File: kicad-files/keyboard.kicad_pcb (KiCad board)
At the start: 2 copper layers, 361.7 x 100 mm, 189 parts, among them J1 TYPE-C-31-M12_13, Q1 2N7002, Q2 2N7002, SW1 K2-1187SQ-A4SW-06, T1 53261-0471, T2 53261-0471, U1 STM32F411CEU6, U2 USBLC6-2SC6, U3 AT24C256C-SSHL-T, U4 SGM2007-3.3XN5/TR, Y1 TAXM8M4RFDCET2T

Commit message: More naming and filleted edge
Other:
- outline, holes or cut-outs redrawn
- board text added: "CAPS_LOCK"
- board text added: "MISC"
- board text added: "TAB"
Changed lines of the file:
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@@
   (gr_line locked (start 162.5 0) (end 162.5 100)
     (stroke (width 0.1) (type default)) (layer "Eco1.User"))
+  (gr_arc (start 1.5 2.1) (mid 2.964466 -1.435534) (end 6.5 -2.9)
+    (stroke (width 0.25) (type default)) (layer "Edge.Cuts"))
+  (gr_line (start 6.5 -2.9) (end 318.5 -2.9)
+    (stroke (width 0.25) (type default)) (layer "Edge.Cuts"))
   (gr_line (start 348.2 61) (end 348.2 36)
     (stroke (width 0.1) (type default)) (layer "Edge.Cuts"))
@@
   (gr_line (start 362.2 62) (end 349.2 62)
     (stroke (width 0.1) (type default)) (layer "Edge.Cuts"))
-  (gr_rect (start 1.5 -2.9) (end 323.5 97.1)
-    (stroke (width 0.25) (type default)) (fill none) (layer "Edge.Cuts"))
   (gr_arc (start 348.2 36) (mid 348.492893 35.292893) (end 349.2 35)
     (stroke (width 0.1) (type default)) (layer "Edge.Cuts"))
+  (gr_line (start 323.5 2.1) (end 323.5 92.1)
+    (stroke (width 0.25) (type default)) (layer "Edge.Cuts"))
+  (gr_arc (start 323.5 92.1) (mid 322.035534 95.635534) (end 318.5 97.1)
+    (stroke (width 0.25) (type default)) (layer "Edge.Cuts"))
   (gr_arc (start 349.2 62) (mid 348.492893 61.707107) (end 348.2 61)
     (stroke (width 0.1) (type default)) (layer "Edge.Cuts"))
   (gr_line (start 363.2 36) (end 363.2 61)
     (stroke (width 0.1) (type default)) (layer "Edge.Cuts"))
+  (gr_arc (start 318.5 -2.9) (mid 322.035534 -1.435534) (end 323.5 2.1)
+    (stroke (width 0.25) (type default)) (layer "Edge.Cuts"))
   (gr_arc (start 363.2 61) (mid 362.907107 61.707107) (end 362.2 62)
     (stroke (width 0.1) (type default)) (layer "Edge.Cuts"))
+  (gr_line (start 1.5 92.1) (end 1.5 2.1)
+    (stroke (width 0.25) (type default)) (layer "Edge.Cuts"))
+  (gr_arc (start 6.5 97.1) (mid 2.964466 95.635534) (end 1.5 92.1)
+    (stroke (width 0.25) (type default)) (layer "Edge.Cuts"))
   (gr_arc (start 362.2 35) (mid 362.907107 35.292893) (end 363.2 36)
     (stroke (width 0.1) (type default)) (layer "Edge.Cuts"))
+  (gr_line (start 318.5 97.1) (end 6.5 97.1)
+    (stroke (width 0.25) (type default)) (layer "Edge.Cuts"))
   (gr_text "HARD RESET" (at 311.5 55.25) (layer "B.SilkS")
     (effects (font (size 0.9 0.9) (thickness 0.2) bold italic) (justify left bottom mirror))
   )
+  (gr_text "TAB\n" (at 21 23.6) (layer "B.SilkS")
+    (effects (font (size 1 1) (thickness 0.15)) (justify left bottom mirror))
+  )
   (gr_text "ALPHA_1" (at 51 4.6) (layer "B.SilkS")
+    (effects (font (size 1 1) (thickness 0.15)) (justify left bottom mirror))
+  )
+  (gr_text "MISC" (at 30.5 43.1) (layer "B.SilkS")
     (effects (font (size 1 1) (thickness 0.15)) (justify left bottom mirror))
   )
@@
     (effects (font (size 1 1) (thickness 0.15)) (justify left bottom mirror))
   )
+  (gr_text "CAPS_LOCK" (at 13.5 43.1) (layer "B.SilkS")
+    (effects (font (size 1 1) (thickness 0.15)) (justify left bottom mirror))
+  )

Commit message: Added more key name soldermask
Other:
- board text added: "Alpha_0"
- board text added: "Alpha_1"
- board text added: "Alpha_2"
- board text added: "Alpha_3"
- board text added: "Alpha_4"
- board text added: "Alpha_5"
- board text added: "Alpha_6"
- board text added: "Alpha_7"
- board text added: "Alpha_8"
- board text added: "Alpha_9"
- board text added: "Backspace"
- board text added: "Capslock"
- board text added: "Dash"
- board text added: "Del"
- board text added: "E"
- board text added: "Equals"
- board text added: "Escape"
- board text added: "Misc"
- board text added: "Q"
- board text added: "R"
- board text added: "Tab"
- board text added: "Tilde"
- board text added: "W"
- board text removed: "ALPHA_1"
- board text removed: "ALPHA_2"
- board text removed: "ALPHA_3"
- board text removed: "CAPS_LOCK"
- board text removed: "ESCAPE"
- board text removed: "MISC"
- board text removed: "TAB"
- board text removed: "TILDE"
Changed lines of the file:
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@@
     (effects (font (size 0.9 0.9) (thickness 0.2) bold italic) (justify left bottom mirror))
   )
-  (gr_text "TAB\n" (at 21 23.6) (layer "B.SilkS")
+  (gr_text "Alpha_4" (at 107.5 4.6) (layer "B.SilkS")
     (effects (font (size 1 1) (thickness 0.15)) (justify left bottom mirror))
   )
-  (gr_text "ALPHA_1" (at 51 4.6) (layer "B.SilkS")
+  (gr_text "Equals" (at 259.5 4.6) (layer "B.SilkS")
     (effects (font (size 1 1) (thickness 0.15)) (justify left bottom mirror))
   )
-  (gr_text "MISC" (at 30.5 43.1) (layer "B.SilkS")
+  (gr_text "Tab" (at 21 23.6) (layer "B.SilkS")
     (effects (font (size 1 1) (thickness 0.15)) (justify left bottom mirror))
   )
-  (gr_text "TILDE" (at 31 4.6) (layer "B.SilkS")
+  (gr_text "Q" (at 48.5 23.1) (layer "B.SilkS")
     (effects (font (size 1 1) (thickness 0.15)) (justify left bottom mirror))
   )
-  (gr_text "ALPHA_3" (at 89 4.6) (layer "B.SilkS")
+  (gr_text "Alpha_1" (at 51 4.6) (layer "B.SilkS")
     (effects (font (size 1 1) (thickness 0.15)) (justify left bottom mirror))
   )
-  (gr_text "ESCAPE" (at 12.5 4.6) (layer "B.SilkS")
+  (gr_text "Backspace" (at 289.5 4.6) (layer "B.SilkS")
     (effects (font (size 1 1) (thickness 0.15)) (justify left bottom mirror))
   )
-  (gr_text "ALPHA_2" (at 70 4.6) (layer "B.SilkS")
+  (gr_text "Misc" (at 30.5 43.1) (layer "B.SilkS")
     (effects (font (size 1 1) (thickness 0.15)) (justify left bottom mirror))
   )
-  (gr_text "CAPS_LOCK" (at 13.5 43.1) (layer "B.SilkS")
+  (gr_text "Tilde" (at 31 4.6) (layer "B.SilkS")
     (effects (font (size 1 1) (thickness 0.15)) (justify left bottom mirror))
   )
+  (gr_text "Alpha_3" (at 89 4.6) (layer "B.SilkS")
+    (effects (font (size 1 1) (thickness 0.15)) (justify left bottom mirror))
+  )
+  (gr_text "Alpha_9" (at 202.5 4.6) (layer "B.SilkS")
+    (effects (font (size 1 1) (thickness 0.15)) (justify left bottom mirror))
+  )
+  (gr_text "Escape" (at 12.5 4.6) (layer "B.SilkS")
+    (effects (font (size 1 1) (thickness 0.15)) (justify left bottom mirror))
+  )
+  (gr_text "E" (at 86.5 23.1) (layer "B.SilkS")
+    (effects (font (size 1 1) (thickness 0.15)) (justify left bottom mirror))
+  )
+  (gr_text "Alpha_5" (at 126.5 4.6) (layer "B.SilkS")
+    (effects (font (size 1 1) (thickness 0.15)) (justify left bottom mirror))
+  )
+  (gr_text "Alpha_6" (at 145.544002 4.544445) (layer "B.SilkS")
+    (effects (font (size 1 1) (thickness 0.15)) (justify left bottom mirror))
+  )
+  (gr_text "Del" (at 316 4.6) (layer "B.SilkS")
+    (effects (font (size 1 1) (thickness 0.15)) (justify left bottom mirror))
+  )
+  (gr_text "R" (at 105.5 23.1) (layer "B.SilkS")
+    (effects (font (size 1 1) (thickness 0.15)) (justify left bottom mirror))
+  )
+  (gr_text "Alpha_0" (at 222 4.6) (layer "B.SilkS")
+    (effects (font (size 1 1) (thickness 0.15)) (justify left bottom mirror))
+  )
+  (gr_text "Alpha_2" (at 70 4.6) (layer "B.SilkS")
+    (effects (font (size 1 1) (thickness 0.15)) (justify left bottom mirror))
+  )
+  (gr_text "Alpha_8" (at 183.5 4.6) (layer "B.SilkS")
+    (effects (font (size 1 1) (thickness 0.15)) (justify left bottom mirror))
+  )
+  (gr_text "Capslock" (at 13 43.1) (layer "B.SilkS")
+    (effects (font (size 1 1) (thickness 0.15)) (justify left bottom mirror))
+  )
+  (gr_text "Dash" (at 241 4.6) (layer "B.SilkS")
+    (effects (font (size 1 1) (thickness 0.15)) (justify left bottom mirror))
+  )
+  (gr_text "W" (at 67.5 23.1) (layer "B.SilkS")
+    (effects (font (size 1 1) (thickness 0.15)) (justify left bottom mirror))
+  )
+  (gr_text "Alpha_7" (at 164.5 4.6) (layer "B.SilkS")
+    (effects (font (size 1 1) (thickness 0.15)) (justify left bottom mirror))
+  )

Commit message: Added more labels
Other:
- board text added: "T"
- board text added: "Y"
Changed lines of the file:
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@@
+    (effects (font (size 1 1) (thickness 0.15)) (justify left bottom mirror))
+  )
+  (gr_text "T" (at 124.5 23.1) (layer "B.SilkS")
     (effects (font (size 1 1) (thickness 0.15)) (justify left bottom mirror))
   )
@@
     (effects (font (size 1 1) (thickness 0.15)) (justify left bottom mirror))
   )
+  (gr_text "Y" (at 144 23.1) (layer "B.SilkS")
+    (effects (font (size 1 1) (thickness 0.15)) (justify left bottom mirror))
+  )

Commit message: Added more labels & Test wire columns
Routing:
- net C0: track 87.7 -> 367.4 mm
- net C1: track 74.6 -> 334.4 mm
- net C2: track 90.7 -> 330.7 mm
- net C3: track 89.3 -> 309.4 mm
- net C4: track 69.0 -> 269.2 mm
- net C5: track 90.9 -> 271.1 mm
- net C6: track 69.0 -> 229.3 mm
- net C7: track 69.0 -> 209.3 mm
- net C8: track 93.4 -> 213.9 mm
- net C9: track 69.0 -> 169.6 mm
- net C10: track 92.2 -> 173.2 mm
- net C11: track 90.6 -> 151.5 mm
- net C12: track 92.0 -> 132.6 mm
- net C13: track 65.1 -> 84.9 mm
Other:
- board text added: "A"
- board text added: "B"
- board text added: "Back Slash"
- board text added: "C"
- board text added: "Colon"
- board text added: "Comma"
- board text added: "D"
- board text added: "Enter"
- board text added: "F"
- board text added: "G"
- board text added: "H"
- board text added: "I"
- board text added: "J"
- board text added: "K"
- board text added: "L"
- board text added: "Left Bracket"
- board text added: "M"
- board text added: "N"
- board text added: "O"
- board text added: "P"
- board text added: "Quote"
- board text added: "Right Bracket"
- board text added: "S"
- board text added: "Shift"
- board text added: "U"
- board text added: "V"
- board text added: "X"
- board text added: "Z"

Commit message: Finished labelling all of the switches
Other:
- board text added: "Alt"
- board text added: "Control"
- board text added: "Down Arrow"
- board text added: "Forward Slash"
- board text added: "Left Arrow"
- board text added: "Period"
- board text added: "Right Arrow"
- board text added: "Space"
- board text added: "Up Arrow"
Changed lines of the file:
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@@
     (effects (font (size 0.9 0.9) (thickness 0.2) bold italic) (justify left bottom mirror))
+  )
+  (gr_text "Misc" (at 245.8 61.9) (layer "B.SilkS")
+    (effects (font (size 1 1) (thickness 0.15)) (justify left bottom mirror))
   )
   (gr_text "Alpha_4" (at 112.5 4.6) (layer "B.SilkS")
     (effects (font (size 1 1) (thickness 0.15)) (justify left bottom mirror))
   )
+  (gr_text "Control" (at 24.4 80.9) (layer "B.SilkS")
+    (effects (font (size 1 1) (thickness 0.15)) (justify left bottom mirror))
+  )
   (gr_text "A" (at 55.3 42.7) (layer "B.SilkS")
+    (effects (font (size 1 1) (thickness 0.15)) (justify left bottom mirror))
+  )
+  (gr_text "Misc" (at 53 80.9) (layer "B.SilkS")
     (effects (font (size 1 1) (thickness 0.15)) (justify left bottom mirror))
   )
@@
     (effects (font (size 1 1) (thickness 0.15)) (justify left bottom mirror))
   )
+  (gr_text "Down Arrow" (at 302.9 80.9) (layer "B.SilkS")
+    (effects (font (size 1 1) (thickness 0.15)) (justify left bottom mirror))
+  )
   (gr_text "Tab" (at 27 23.6) (layer "B.SilkS")
     (effects (font (size 1 1) (thickness 0.15)) (justify left bottom mirror))
   )
-  (gr_text "Comma" (at 207.8 61.9) (layer "B.SilkS")
+  (gr_text "Up Arrow" (at 302 61.8) (layer "B.SilkS")
+    (effects (font (size 1 1) (thickness 0.15)) (justify left bottom mirror))
+  )
+  (gr_text "Period" (at 207.8 61.9) (layer "B.SilkS")
     (effects (font (size 1 1) (thickness 0.15)) (justify left bottom mirror))
   )
@@
     (effects (font (size 1 1) (thickness 0.15)) (justify left bottom mirror))
   )
+  (gr_text "Alt" (at 200.6 80.9) (layer "B.SilkS")
+    (effects (font (size 1 1) (thickness 0.15)) (justify left bottom mirror))
+  )
   (gr_text "Q" (at 55.25 23.6) (layer "B.SilkS")
     (effects (font (size 1 1) (thickness 0.15)) (justify left bottom mirror))
@@
     (effects (font (size 1 1) (thickness 0.15)) (justify left bottom mirror))
   )
+  (gr_text "Space" (at 160.1 80.9) (layer "B.SilkS")
+    (effects (font (size 1 1) (thickness 0.15)) (justify left bottom mirror))
+  )
+  (gr_text "Forward Slash" (at 226.8 61.9) (layer "B.SilkS")
+    (effects (font (size 1 1) (thickness 0.15)) (justify left bottom mirror))
+  )
   (gr_text "Misc" (at 322.1 23.5) (layer "B.SilkS")
     (effects (font (size 1 1) (thickness 0.15)) (justify left bottom mirror))
@@
     (effects (font (size 1 1) (thickness 0.15)) (justify left bottom mirror))
   )
+  (gr_text "Alt" (at 76.7 80.9) (layer "B.SilkS")
+    (effects (font (size 1 1) (thickness 0.15)) (justify left bottom mirror))
+  )
+  (gr_text "Misc" (at 264.8 61.9) (layer "B.SilkS")
+    (effects (font (size 1 1) (thickness 0.15)) (justify left bottom mirror))
+  )
   (gr_text "Misc" (at 36.2 42.7) (layer "B.SilkS")
     (effects (font (size 1 1) (thickness 0.15)) (justify left bottom mirror))
@@
     (effects (font (size 1 1) (thickness 0.15)) (justify left bottom mirror))
   )
+  (gr_text "Misc" (at 224.4 80.9) (layer "B.SilkS")
+    (effects (font (size 1 1) (thickness 0.15)) (justify left bottom mirror))
+  )
   (gr_text "Tilde" (at 36.5 4.6) (layer "B.SilkS")
     (effects (font (size 1 1) (thickness 0.15)) (justify left bottom mirror))
   )
   (gr_text "P" (at 226.75 23.6) (layer "B.SilkS")
+    (effects (font (size 1 1) (thickness 0.15)) (justify left bottom mirror))
+  )
+  (gr_text "Right Arrow" (at 322 80.9) (layer "B.SilkS")
     (effects (font (size 1 1) (thickness 0.15)) (justify left bottom mirror))
   )
@@
     (effects (font (size 1 1) (thickness 0.15)) (justify left bottom mirror))
   )
+  (gr_text "Misc" (at 245.8 80.9) (layer "B.SilkS")
+    (effects (font (size 1 1) (thickness 0.15)) (justify left bottom mirror))
+  )
   (gr_text "Back Slash" (at 284 23.5) (layer "B.SilkS")
     (effects (font (size 1 1) (thickness 0.15)) (justify left bottom mirror))
@@
   )
   (gr_text "B" (at 131.5 61.8) (layer "B.SilkS")
+    (effects (font (size 1 1) (thickness 0.15)) (justify left bottom mirror))
+  )
+  (gr_text "Misc" (at 110 80.9) (layer "B.SilkS")
     (effects (font (size 1 1) (thickness 0.15)) (justify left bottom mirror))
   )
@@
     (effects (font (size 1 1) (thickness 0.15)) (justify left bottom mirror))
   )
+  (gr_text "Left Arrow" (at 283.9 80.9) (layer "B.SilkS")
+    (effects (font (size 1 1) (thickness 0.15)) (justify left bottom mirror))
+  )

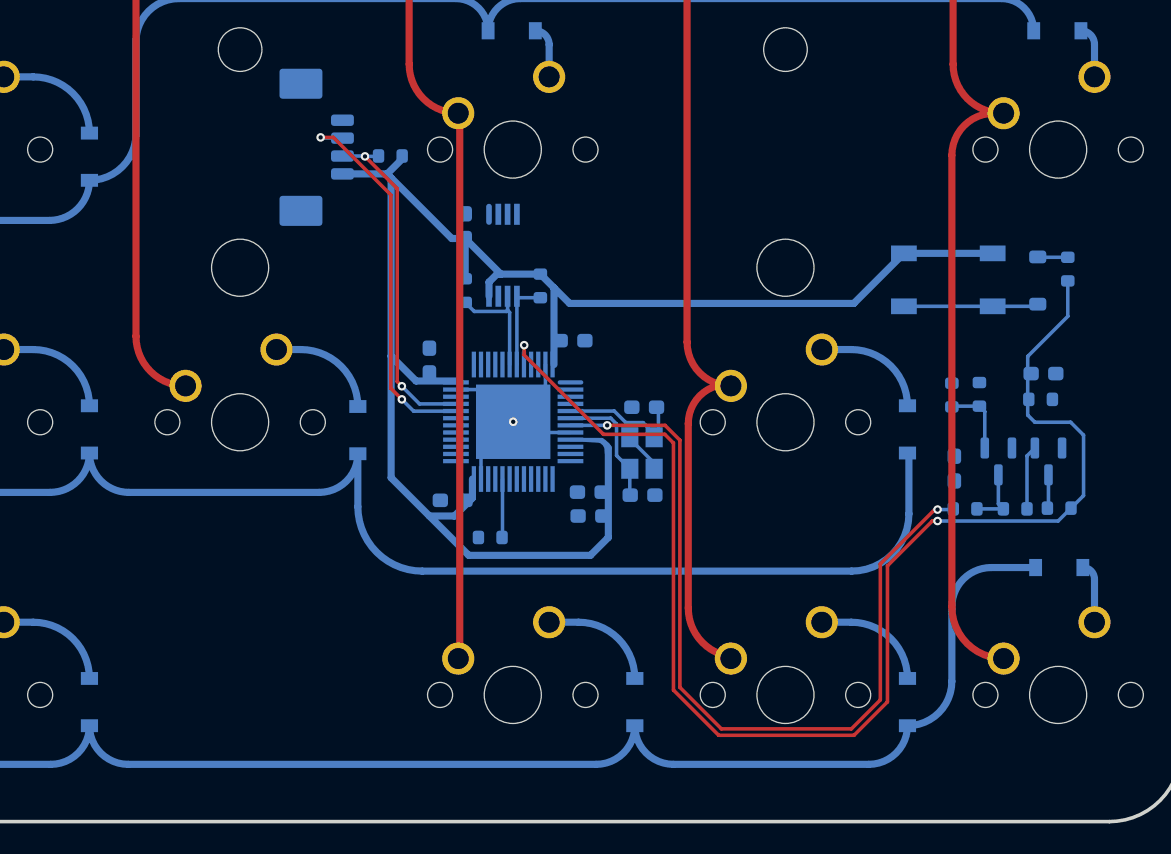
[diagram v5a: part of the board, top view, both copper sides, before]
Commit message: Moved the reset swtich
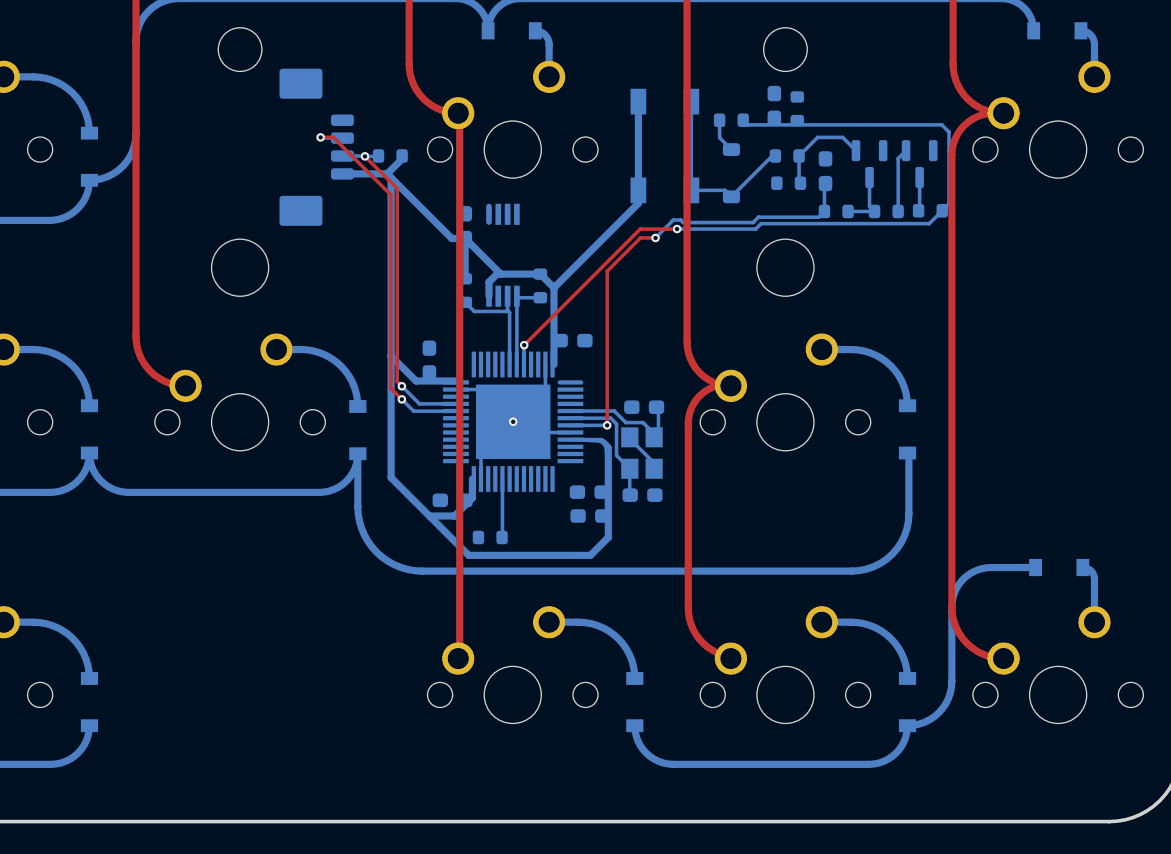
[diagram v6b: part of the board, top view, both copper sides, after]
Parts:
- moved C8 26.5 mm to (295.1, 47.1), turned to 90 degrees
- moved R14 26.5 mm to (296.7, 47.3), turned to 90 degrees
- moved R13 25.7 mm to (292.1, 48.1), turned to 180 degrees
- moved D_72 22.7 mm to (292.1, 51.8)
- moved R15 22.6 mm to (306.0, 54.4)
- moved C7 22.6 mm to (298.7, 51.7)
- moved Q1 22.6 mm to (301.8, 51.2)
- moved Q2 22.6 mm to (305.2, 51.2)
- moved R11 22.6 mm to (302.9, 54.5)
- moved R12 22.6 mm to (299.4, 54.5)
- moved SW1 21.9 mm to (287.4, 49.9), turned to -90 degrees
- moved R9 21.4 mm to (296.0, 50.6), turned to 180 degrees
- moved R10 18.7 mm to (296.1, 52.5), turned to 180 degrees
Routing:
- net R4: track 321.9 -> 280.9 mm
- net Net-(U1-BOOT0): track 94.1 -> 55.0 mm
- net Net-(U1-NRST): track 59.6 -> 32.4 mm
- net 3V3: track 120.6 -> 103.5 mm
- net Net-(D_72-A): track 9.41 -> 13.4 mm
- net Net-(Q1-G): track 4.89 -> 6.84 mm
